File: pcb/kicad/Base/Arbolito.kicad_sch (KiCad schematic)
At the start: 68 parts, among them J1 Battery, J10 Conn_01x01, J11 Conn_01x01, J12 Conn_01x01, J13 Conn_01x01, J14 Conn_01x01, J2 Conn_01x06_Female, J3 Conn_01x01, J4 Conn_01x01, J5 Conn_01x01, J6 Conn_01x01, J7 Conn_01x01, J8 Conn_01x01, J9 Conn_01x01, P1 TYPE-C 16PIN 2MD(073), Q1 S8050, Q2 S8050, Q3 S8050, SW1 SW_DP3T, SW2 SW_Push, SW3 SW_Push, SW4 SW_Push, U1 NCP115AMX120TCG, U2 CH340C, U3 AP63205WU, U4 ESP-12F, U5 SHT31-DIS

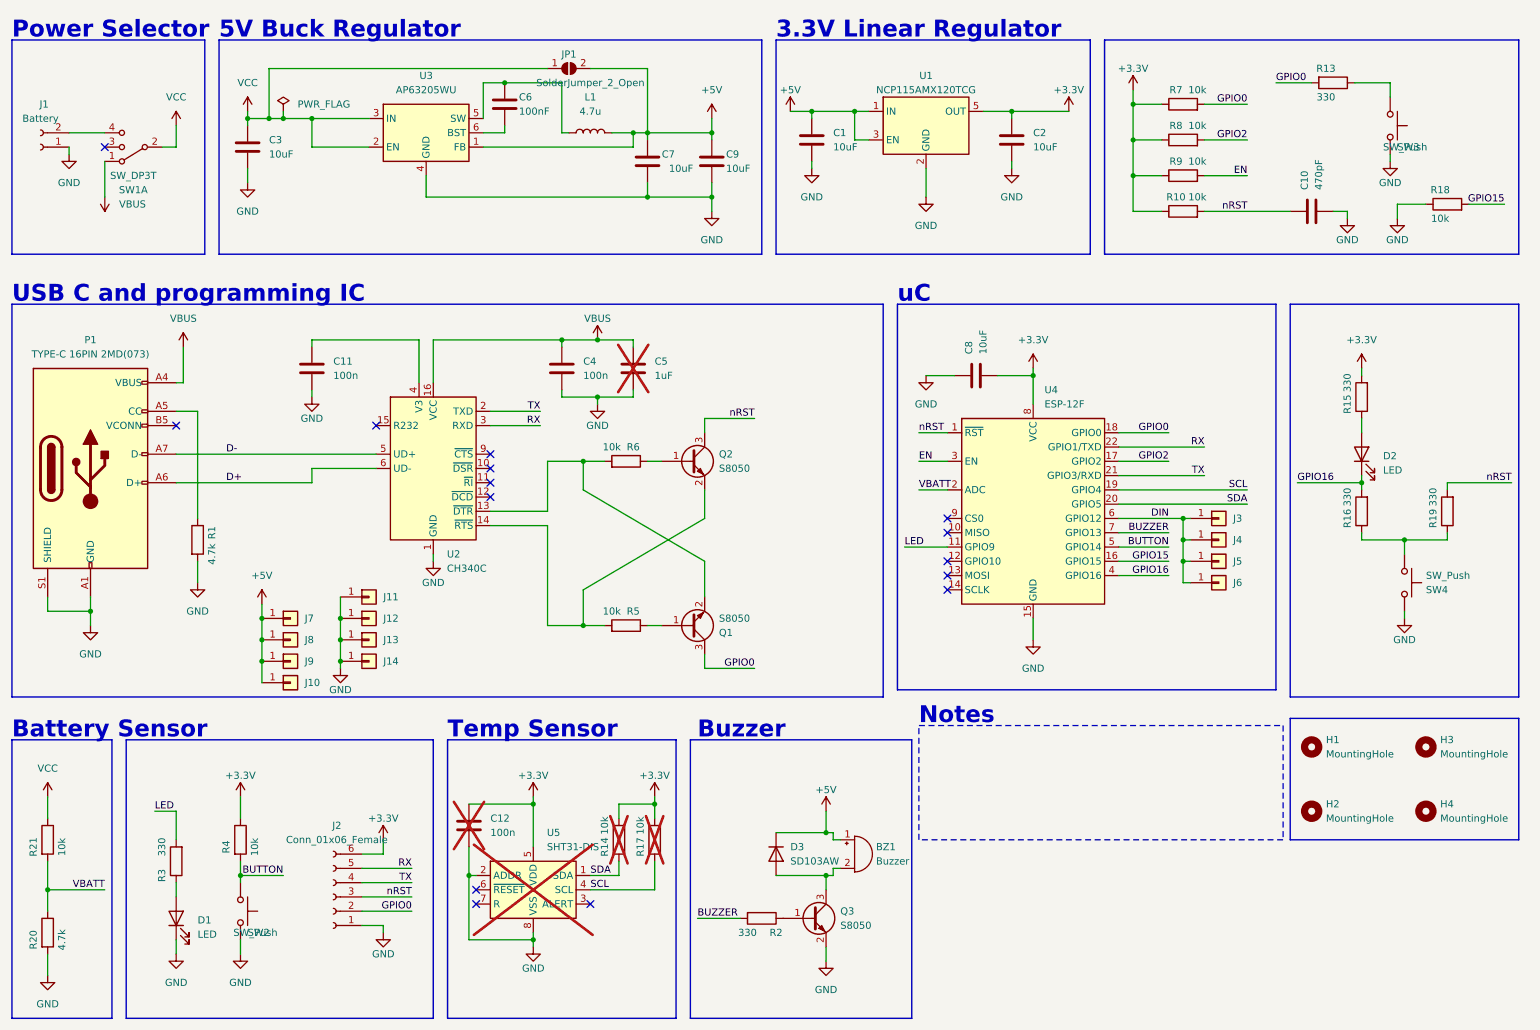
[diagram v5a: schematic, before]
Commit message: Added Rev3 release files
- Added ibom html files
- Update ibom in .web directory
- Update pdf schematics
- Added 3D steps files
- Added tools for help to mount the PCB
- Added hw rev3 gerber files
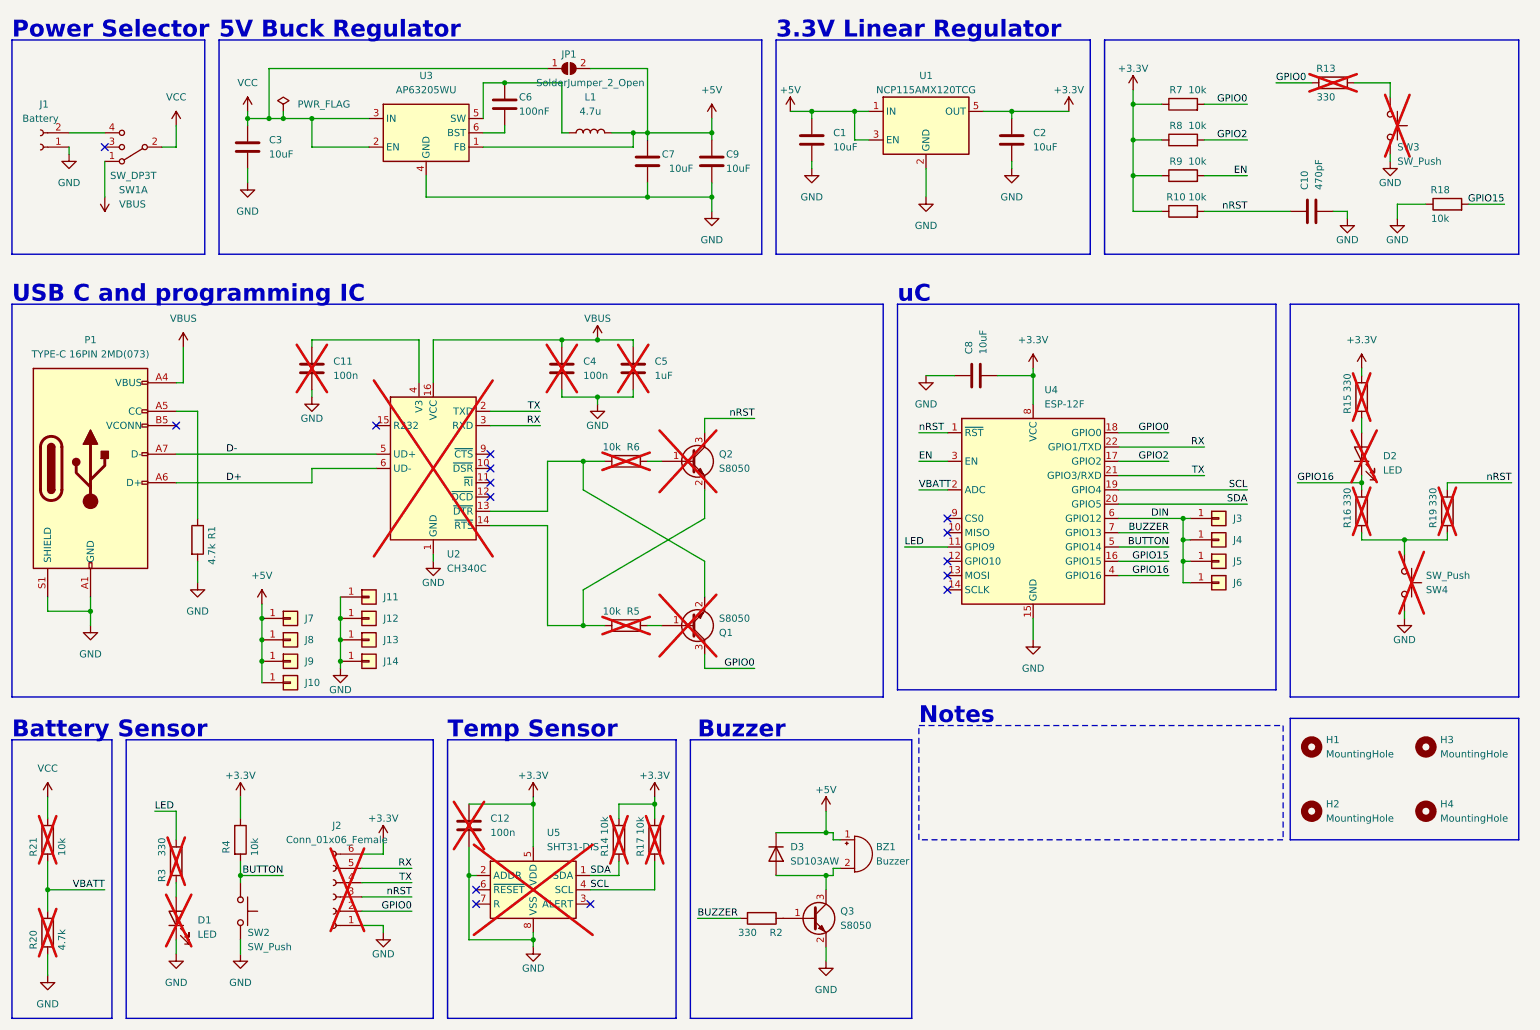
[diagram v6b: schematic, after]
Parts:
- C11, C4, D1, D2, J2, Q1, Q2, R13, R15, R16, R19, R20, R21, R3, R5, R6, SW3, SW4, U2: now not fitted
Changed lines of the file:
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@@
   )
   (symbol (lib_id "Device:R") (at 255.27 85.09 180) (unit 1)
-    (in_bom yes) (on_board yes) (dnp no)
+    (in_bom yes) (on_board yes) (dnp yes)
     (property "Reference" "R15" (at 252.73 86.36 90)
       (effects (font (size 1.27 1.27)))
@@
     )
     (property "Datasheet" "https://www.sensirion.com/fileadmin/user_upload/customers/sensirion/Dokumente/2_Humidity_Sensors/Datasheets/Sensirion_Humidity_Sensors_SHT3x_Datasheet_digital.pdf" (at 107.95 171.45 0)
-      (effects (font (size 1.27 1.27)) hide)
-    )
-    (property "dnp" "" (at 107.95 172.72 0)
-      (effects (font (size 1.27 1.27)) hide)
-    )
-    (property "Field5" "" (at 107.95 172.72 0)
       (effects (font (size 1.27 1.27)) hide)
     )
@@
   )
   (symbol (lib_id "Device:R") (at 124.46 96.52 270) (mirror x) (unit 1)
-    (in_bom yes) (on_board yes) (dnp no)
+    (in_bom yes) (on_board yes) (dnp yes)
     (property "Reference" "R6" (at 125.73 93.98 90)
       (effects (font (size 1.27 1.27)))
@@
   )
   (symbol (lib_name "S8050_1") (lib_id "Transistor_BJT:S8050") (at 135.89 125.73 0) (mirror x) (unit 1)
-    (in_bom yes) (on_board yes) (dnp no) (fields_autoplaced)
+    (in_bom yes) (on_board yes) (dnp yes) (fields_autoplaced)
     (property "Reference" "Q1" (at 140.97 127.0001 0)
       (effects (font (size 1.27 1.27)) (justify left))
@@
   )
   (symbol (lib_id "Device:R") (at 124.46 125.73 270) (mirror x) (unit 1)
-    (in_bom yes) (on_board yes) (dnp no)
+    (in_bom yes) (on_board yes) (dnp yes)
     (property "Reference" "R5" (at 125.73 123.19 90)
       (effects (font (size 1.27 1.27)))
@@
   )
   (symbol (lib_id "Interface_USB:CH340C") (at 90.17 97.79 0) (unit 1)
-    (in_bom yes) (on_board yes) (dnp no) (fields_autoplaced)
+    (in_bom yes) (on_board yes) (dnp yes) (fields_autoplaced)
     (property "Reference" "U2" (at 92.5956 113.03 0)
       (effects (font (size 1.27 1.27)) (justify left))
@@
   )
   (symbol (lib_id "Device:R") (at 21.59 180.34 0) (unit 1)
-    (in_bom yes) (on_board yes) (dnp no)
+    (in_bom yes) (on_board yes) (dnp yes)
     (property "Reference" "R20" (at 19.05 181.61 90)
       (effects (font (size 1.27 1.27)))
@@
   )
   (symbol (lib_id "Switch:SW_Push") (at 260.35 36.83 270) (unit 1)
-    (in_bom yes) (on_board yes) (dnp no) (fields_autoplaced)
+    (in_bom yes) (on_board yes) (dnp yes)
     (property "Reference" "SW3" (at 261.6201 40.64 90)
       (effects (font (size 1.27 1.27)) (justify left))
     )
-    (property "Value" "SW_Push" (at 259.0801 40.64 90)
+    (property "Value" "SW_Push" (at 261.62 43.18 90)
       (effects (font (size 1.27 1.27)) (justify left))
     )
@@
   )
   (symbol (lib_id "Device:R") (at 44.45 167.64 180) (unit 1)
-    (in_bom yes) (on_board yes) (dnp no)
+    (in_bom yes) (on_board yes) (dnp yes)
     (property "Reference" "R3" (at 41.91 170.18 90)
       (effects (font (size 1.27 1.27)))
@@
   )
   (symbol (lib_name "SW_Push_2") (lib_id "Switch:SW_Push") (at 55.88 176.53 270) (unit 1)
-    (in_bom yes) (on_board yes) (dnp no) (fields_autoplaced)
+    (in_bom yes) (on_board yes) (dnp no)
     (property "Reference" "SW2" (at 57.1501 180.34 90)
       (effects (font (size 1.27 1.27)) (justify left))
     )
-    (property "Value" "SW_Push" (at 54.6101 180.34 90)
+    (property "Value" "SW_Push" (at 57.15 182.88 90)
       (effects (font (size 1.27 1.27)) (justify left))
     )
@@
   )
   (symbol (lib_id "Device:C") (at 68.58 80.01 0) (unit 1)
-    (in_bom yes) (on_board yes) (dnp no) (fields_autoplaced)
+    (in_bom yes) (on_board yes) (dnp yes) (fields_autoplaced)
     (property "Reference" "C11" (at 72.39 78.7399 0)
       (effects (font (size 1.27 1.27)) (justify left))
@@
   )
   (symbol (lib_id "Connector:Conn_01x06_Female") (at 72.39 173.99 180) (unit 1)
-    (in_bom yes) (on_board yes) (dnp no)
+    (in_bom yes) (on_board yes) (dnp yes)
     (property "Reference" "J2" (at 73.025 161.29 0)
       (effects (font (size 1.27 1.27)))
@@
   )
   (symbol (lib_id "Device:LED") (at 255.27 95.25 90) (unit 1)
-    (in_bom yes) (on_board yes) (dnp no) (fields_autoplaced)
+    (in_bom yes) (on_board yes) (dnp yes) (fields_autoplaced)
     (property "Reference" "D2" (at 259.08 95.5674 90)
       (effects (font (size 1.27 1.27)) (justify right))
@@
   )
   (symbol (lib_id "Device:R") (at 250.19 29.21 270) (unit 1)
-    (in_bom yes) (on_board yes) (dnp no)
+    (in_bom yes) (on_board yes) (dnp yes)
     (property "Reference" "R13" (at 248.92 26.67 90)
       (effects (font (size 1.27 1.27)))
@@
   )
   (symbol (lib_id "Device:LED") (at 44.45 177.8 90) (unit 1)
-    (in_bom yes) (on_board yes) (dnp no) (fields_autoplaced)
+    (in_bom yes) (on_board yes) (dnp yes) (fields_autoplaced)
     (property "Reference" "D1" (at 48.26 178.1174 90)
       (effects (font (size 1.27 1.27)) (justify right))
@@
   )
   (symbol (lib_id "Device:C") (at 113.03 80.01 0) (unit 1)
-    (in_bom yes) (on_board yes) (dnp no) (fields_autoplaced)
+    (in_bom yes) (on_board yes) (dnp yes) (fields_autoplaced)
     (property "Reference" "C4" (at 116.84 78.7399 0)
       (effects (font (size 1.27 1.27)) (justify left))
@@
   )
   (symbol (lib_id "Device:R") (at 255.27 105.41 180) (unit 1)
-    (in_bom yes) (on_board yes) (dnp no)
+    (in_bom yes) (on_board yes) (dnp yes)
     (property "Reference" "R16" (at 252.73 106.68 90)
       (effects (font (size 1.27 1.27)))
@@
   )
   (symbol (lib_id "Device:R") (at 21.59 163.83 0) (unit 1)
-    (in_bom yes) (on_board yes) (dnp no)
+    (in_bom yes) (on_board yes) (dnp yes)
     (property "Reference" "R21" (at 19.05 165.1 90)
       (effects (font (size 1.27 1.27)))
@@
   )
   (symbol (lib_name "SW_Push_1") (lib_id "Switch:SW_Push") (at 262.89 118.11 270) (unit 1)
-    (in_bom yes) (on_board yes) (dnp no)
+    (in_bom yes) (on_board yes) (dnp yes)
     (property "Reference" "SW4" (at 266.7 119.38 90)
       (effects (font (size 1.27 1.27)) (justify left))
@@
   )
   (symbol (lib_name "S8050_1") (lib_id "Transistor_BJT:S8050") (at 135.89 96.52 0) (unit 1)
-    (in_bom yes) (on_board yes) (dnp no)
+    (in_bom yes) (on_board yes) (dnp yes)
     (property "Reference" "Q2" (at 140.97 95.2499 0)
       (effects (font (size 1.27 1.27)) (justify left))
@@
   )
   (symbol (lib_id "Device:R") (at 270.51 105.41 180) (unit 1)
-    (in_bom yes) (on_board yes) (dnp no)
+    (in_bom yes) (on_board yes) (dnp yes)
     (property "Reference" "R19" (at 267.97 106.68 90)
       (effects (font (size 1.27 1.27)))

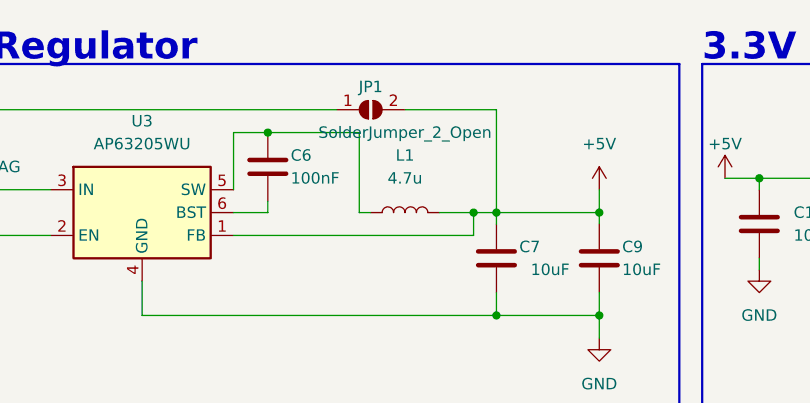
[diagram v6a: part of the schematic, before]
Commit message: Modify ibom html and added WLED binary files
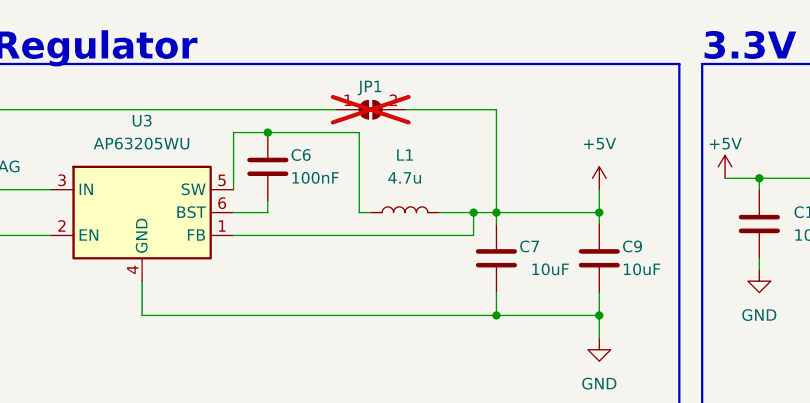
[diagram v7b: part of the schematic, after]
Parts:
- JP1: now not fitted
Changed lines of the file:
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@@
   )
   (symbol (lib_id "Jumper:SolderJumper_2_Open") (at 114.3 26.67 0) (unit 1)
-    (in_bom yes) (on_board yes) (dnp no)
+    (in_bom yes) (on_board yes) (dnp yes)
     (property "Reference" "JP1" (at 114.3 24.13 0)
       (effects (font (size 1.27 1.27)))
     )
     (property "Value" "SolderJumper_2_Open" (at 118.11 29.21 0)
-      (effects (font (size 1.27 1.27)))
+      (effects (font (size 1.27 1.27)) hide)
     )
     (property "Footprint" "Jumper:SolderJumper-2_P1.3mm_Open_RoundedPad1.0x1.5mm" (at 114.3 26.67 0)
